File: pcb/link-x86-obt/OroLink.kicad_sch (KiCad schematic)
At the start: 7 parts, among them J1 67996-408HLF

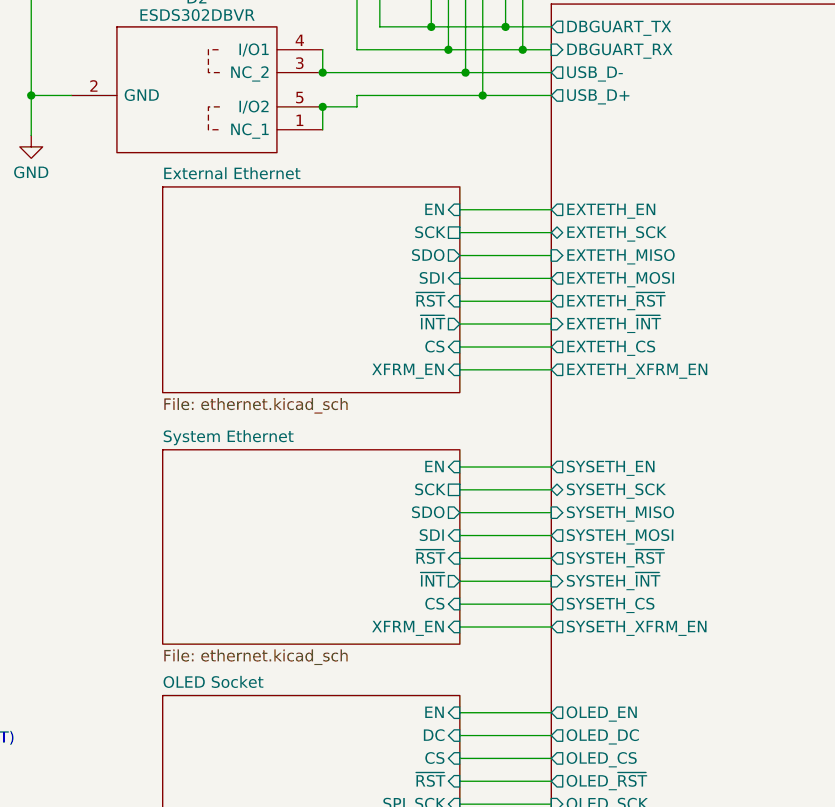
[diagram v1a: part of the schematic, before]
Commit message: omit ethernet enable mosfets in lieu of reset mosfet
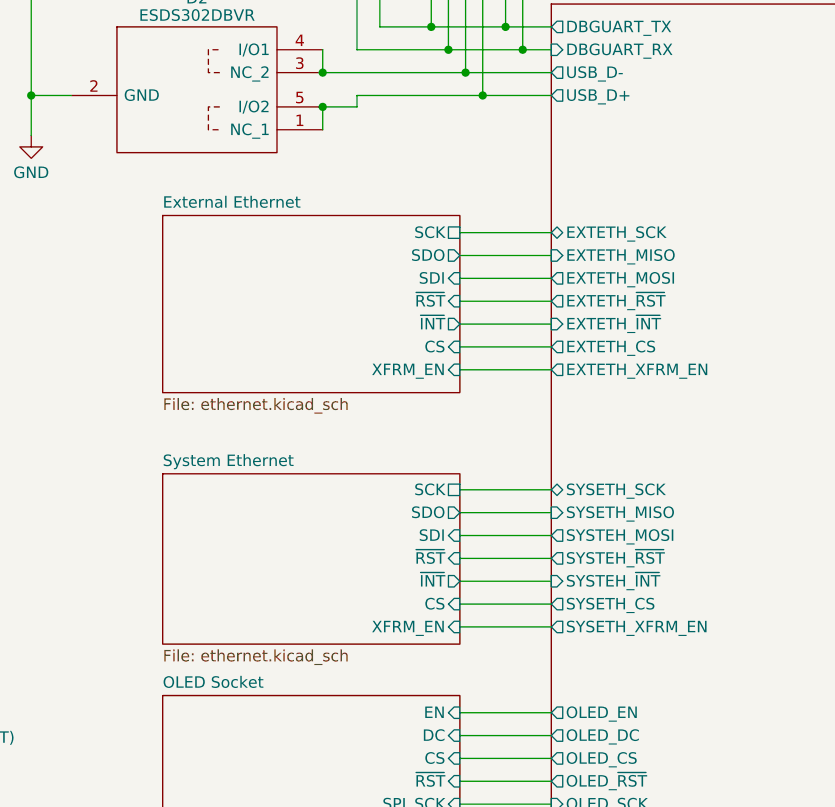
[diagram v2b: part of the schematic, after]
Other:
- sheet External Ethernet ports: added none; removed EN
- sheet Microcontroller ports: added none; removed EXTETH_EN, SYSETH_EN
- sheet System Ethernet ports: added none; removed EN
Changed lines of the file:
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@@
-	(wire
-		(pts
-			(xy 114.3 105.41) (xy 124.46 105.41)
-		)
-		(stroke
-			(width 0)
-			(type default)
-		)
-	)
 	(wire
 		(pts
@@
 		(pts
 			(xy 102.87 65.405) (xy 99.06 65.405)
-		)
-		(stroke
-			(width 0)
-			(type default)
-		)
-	)
-	(wire
-		(pts
-			(xy 114.3 76.835) (xy 124.46 76.835)
 		)
 		(stroke
@@
 	)
 	(sheet
-		(at 81.28 103.505)
-		(size 33.02 21.59)
+		(at 81.28 106.172)
+		(size 33.02 18.923)
 		(fields_autoplaced yes)
 		(stroke
@@
 		)
 		(property "Sheetname" "System Ethernet"
-			(at 81.28 102.7934 0)
+			(at 81.28 105.4604 0)
 			(effects
 				(font
@@
 		(pin "XFRM_EN" input
 			(at 114.3 123.19 0)
-			(effects
-				(font
-					(size 1.27 1.27)
-				)
-				(justify right)
-			)
-		)
-		(pin "EN" input
-			(at 114.3 105.41 0)
 			(effects
 				(font
@@
 	)
 	(sheet
-		(at 81.28 74.295)
-		(size 33.02 22.86)
+		(at 81.28 77.47)
+		(size 33.02 19.685)
 		(fields_autoplaced yes)
 		(stroke
@@
 		)
 		(property "Sheetname" "External Ethernet"
-			(at 81.28 73.5834 0)
+			(at 81.28 76.7584 0)
 			(effects
 				(font
@@
 		(pin "XFRM_EN" input
 			(at 114.3 94.615 0)
-			(effects
-				(font
-					(size 1.27 1.27)
-				)
-				(justify right)
-			)
-		)
-		(pin "EN" input
-			(at 114.3 76.835 0)
 			(effects
 				(font
@@
 			)
 		)
-		(pin "EXTETH_EN" output
-			(at 124.46 76.835 180)
-			(effects
-				(font
-					(size 1.27 1.27)
-				)
-				(justify left)
-			)
-		)
-		(pin "SYSETH_EN" output
-			(at 124.46 105.41 180)
-			(effects
-				(font
-					(size 1.27 1.27)
-				)
-				(justify left)
-			)
-		)

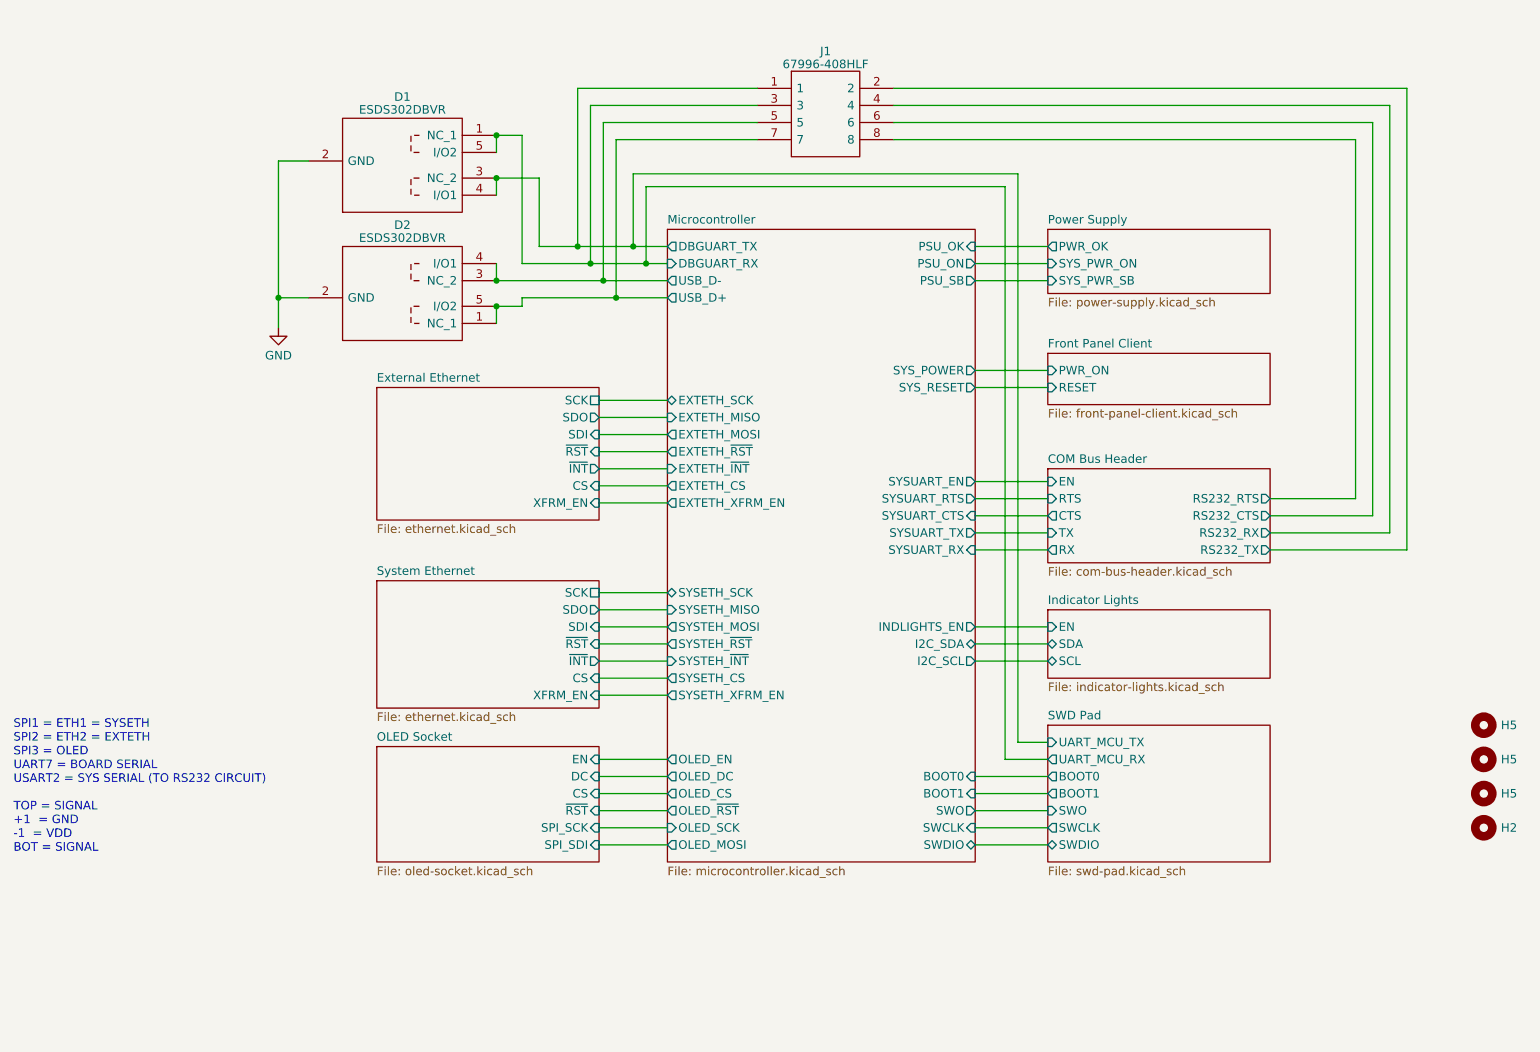
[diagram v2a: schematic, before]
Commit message: add VBUS and ground headers
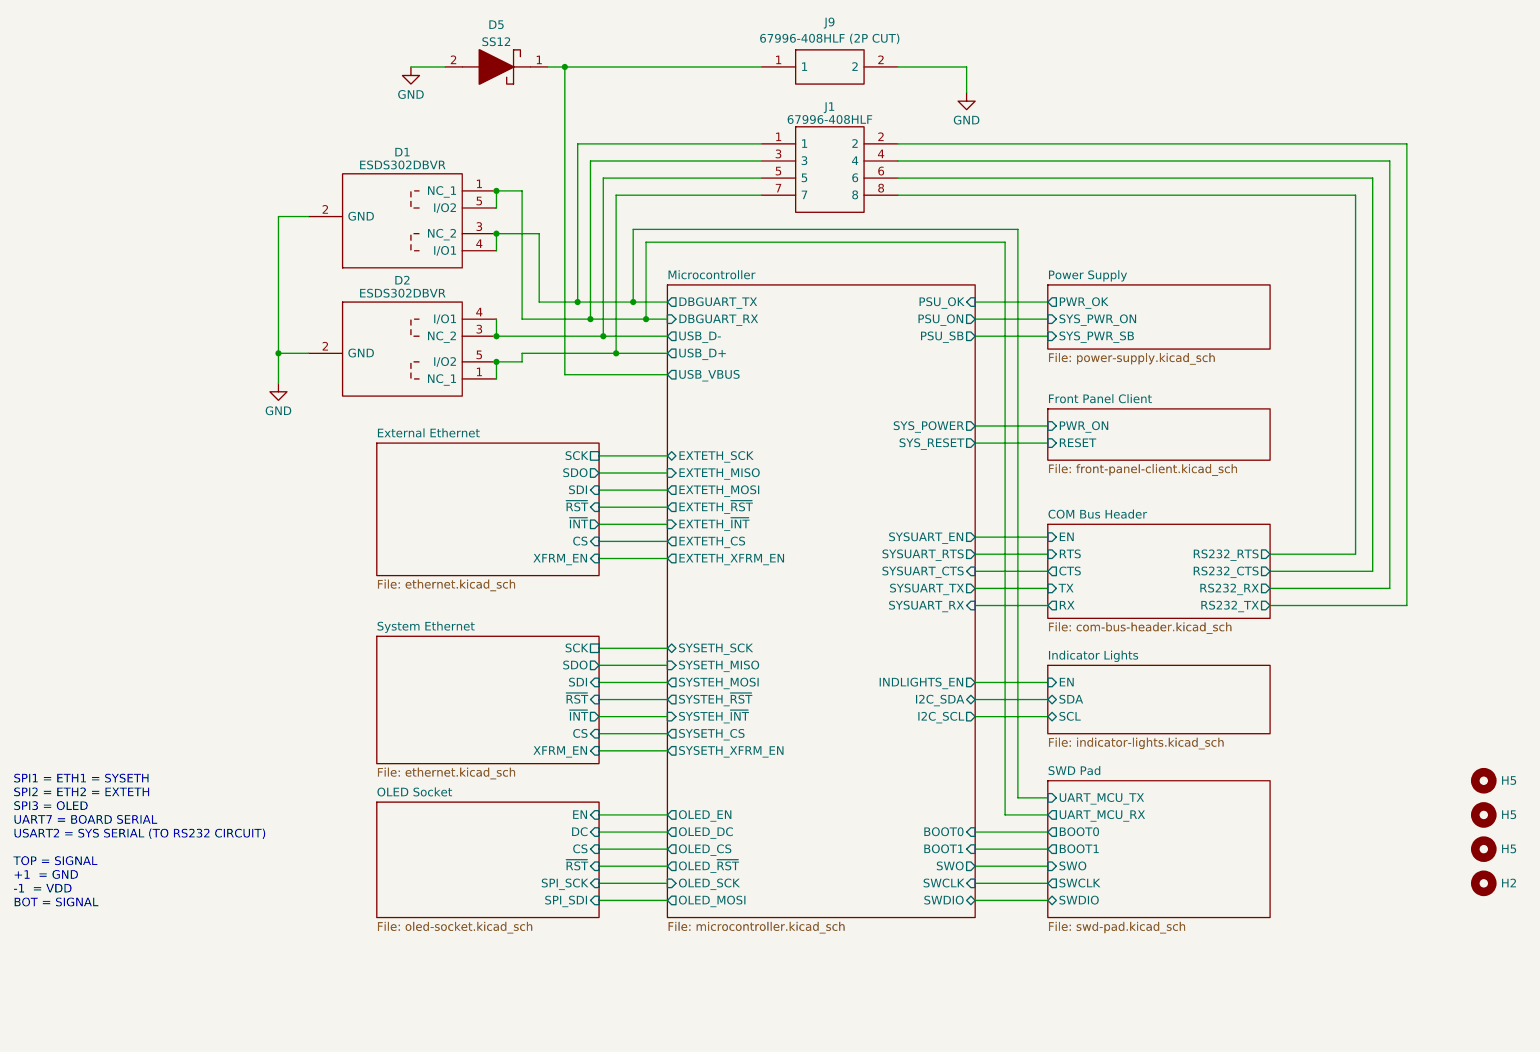
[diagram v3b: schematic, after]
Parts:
- added D5: SS12, Oro Footprints:DIOM5227X250N, symbol SamacSys_Parts:SS12
- added J9: 67996-408HLF (2P CUT), Oro Footprints:HDRV8W89P254_2X4_1016X483X858P_2P, symbol Oro (Legacy):67996-408HLF (2P Cut)
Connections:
- net GND: now also D5.2, J9.2
- new net Microcontroller/USB_VBUS: D5.1, J9.1
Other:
- sheet Microcontroller ports: added USB_VBUS; removed none
- moved on the sheet: D1, D2, H2, H5, J1

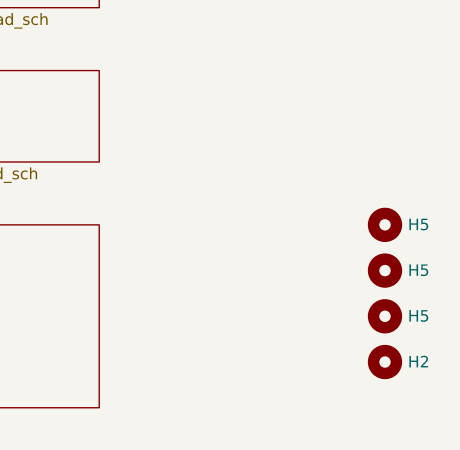
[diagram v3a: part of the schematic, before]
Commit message: make top right mounting hole grounded (closes #51)
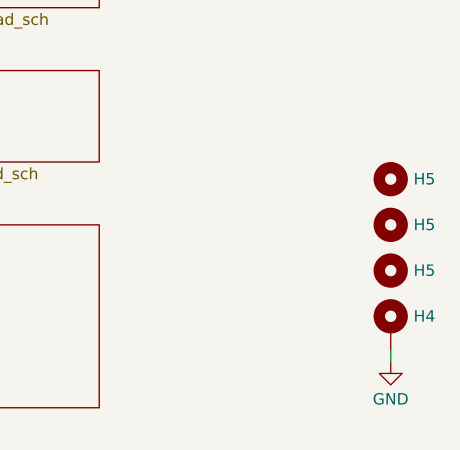
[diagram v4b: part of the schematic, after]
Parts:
- removed H2: MountingHole_Pad, MountingHole:MountingHole_3.2mm_M3_Pad_Via, symbol Mechanical:MountingHole
- added H4: MountingHole_Pad, MountingHole:MountingHole_3.2mm_M3_Pad_Via, symbol Mechanical:MountingHole_Pad
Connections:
- net GND: now also H4.1
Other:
- moved on the sheet: H5
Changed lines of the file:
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@@
+	(wire
+		(pts
+			(xy 246.38 149.86) (xy 246.38 151.13)
+		)
+		(stroke
+			(width 0)
+			(type default)
+		)
+	)
 	(wire
 		(pts
@@
 	(symbol
 		(lib_id "Mechanical:MountingHole")
-		(at 245.745 146.05 0)
+		(at 246.38 140.97 0)
 		(unit 1)
 		(exclude_from_sim yes)
@@
 		(dnp no)
 		(property "Reference" "H5"
-			(at 248.285 146.05 0)
+			(at 248.92 140.97 0)
 			(effects
 				(font
@@
 		)
 		(property "Value" "MountingHole_Pad"
-			(at 248.285 146.0573 0)
+			(at 248.92 140.9773 0)
 			(effects
 				(font
@@
 		)
 		(property "Footprint" "MountingHole:MountingHole_3.2mm_M3_Pad_Via"
-			(at 245.745 146.05 0)
+			(at 246.38 140.97 0)
 			(effects
 				(font
@@
 		)
 		(property "Datasheet" "~"
-			(at 245.745 146.05 0)
+			(at 246.38 140.97 0)
 			(effects
 				(font
@@
 		)
 		(property "Description" ""
-			(at 245.745 146.05 0)
+			(at 246.38 140.97 0)
 			(effects
 				(font
@@
 	(symbol
 		(lib_id "Mechanical:MountingHole")
-		(at 245.745 140.97 0)
+		(at 246.38 135.89 0)
 		(unit 1)
 		(exclude_from_sim yes)
@@
 		(dnp no)
 		(property "Reference" "H5"
-			(at 248.285 140.97 0)
+			(at 248.92 135.89 0)
 			(effects
 				(font
@@
 		)
 		(property "Value" "MountingHole_Pad"
-			(at 248.285 140.9773 0)
+			(at 248.92 135.8973 0)
 			(effects
 				(font
@@
 		)
 		(property "Footprint" "MountingHole:MountingHole_3.2mm_M3_Pad_Via"
-			(at 245.745 140.97 0)
+			(at 246.38 135.89 0)
 			(effects
 				(font
@@
 		)
 		(property "Datasheet" "~"
-			(at 245.745 140.97 0)
+			(at 246.38 135.89 0)
 			(effects
 				(font
@@
 		)
 		(property "Description" ""
-			(at 245.745 140.97 0)
+			(at 246.38 135.89 0)
 			(effects
 				(font
@@
 	(symbol
 		(lib_id "Mechanical:MountingHole")
-		(at 245.745 135.89 0)
+		(at 246.38 130.81 0)
 		(unit 1)
 		(exclude_from_sim yes)
@@
 		(dnp no)
 		(property "Reference" "H5"
-			(at 248.285 135.89 0)
+			(at 248.92 130.81 0)
 			(effects
 				(font
@@
 		)
 		(property "Value" "MountingHole_Pad"
-			(at 248.285 135.8973 0)
+			(at 248.92 130.8173 0)
 			(effects
 				(font
@@
 		)
 		(property "Footprint" "MountingHole:MountingHole_3.2mm_M3_Pad_Via"
-			(at 245.745 135.89 0)
+			(at 246.38 130.81 0)
 			(effects
 				(font
@@
 		)
 		(property "Datasheet" "~"
-			(at 245.745 135.89 0)
+			(at 246.38 130.81 0)
 			(effects
 				(font
@@
 		)
 		(property "Description" ""
-			(at 245.745 135.89 0)
+			(at 246.38 130.81 0)
 			(effects
 				(font
@@
 	)
 	(symbol
-		(lib_id "Mechanical:MountingHole")
-		(at 245.745 151.13 0)
-		(unit 1)
-		(exclude_from_sim yes)
-		(in_bom no)
-		(on_board yes)
-		(dnp no)
-		(property "Reference" "H2"
-			(at 248.285 151.1387 0)
-			(effects
-				(font
-					(size 1.27 1.27)
-				)
-				(justify left)
-			)
-		)
-		(property "Value" "MountingHole_Pad"
-			(at 248.285 151.1373 0)
-			(effects
-				(font
-					(size 1.27 1.27)
-				)
-				(justify left)
-				(hide yes)
-			)
-		)
-		(property "Footprint" "MountingHole:MountingHole_3.2mm_M3_Pad_Via"
-			(at 245.745 151.13 0)
-			(effects
-				(font
-					(size 1.27 1.27)
-				)
-				(hide yes)
-			)
-		)
-		(property "Datasheet" "~"
-			(at 245.745 151.13 0)
-			(effects
-				(font
-					(size 1.27 1.27)
-				)
-				(hide yes)
-			)
-		)
-		(property "Description" ""
-			(at 245.745 151.13 0)
-			(effects
-				(font
-					(size 1.27 1.27)
-				)
-				(hide yes)
-			)
-		)
-		(instances
-			(project "Oro Testbed v2"
-				(path "/3d0fc623-63eb-45e5-a304-e470d9b3a173"
-					(reference "H2")
-					(unit 1)
-				)
-			)
-			(project "OroLink"
-				(path "/e89dcd22-1250-4a5b-b778-1c95a0dd623d"
-					(reference "H4")
-					(unit 1)
-				)
-			)
-		)
-	)
-	(symbol
 		(lib_id "SamacSys_Parts:67996-408HLF")
 		(at 138.43 41.275 0)
@@
 					(unit 1)
 				)
+			)
+		)
+	)
+	(symbol
+		(lib_name "GND_1")
+		(lib_id "power:GND")
+		(at 246.38 151.13 0)
+		(unit 1)
+		(exclude_from_sim no)
+		(in_bom yes)
+		(on_board yes)
+		(dnp no)
+		(fields_autoplaced yes)
+		(property "Reference" "#PWR088"
+			(at 246.38 157.48 0)
+			(effects
+				(font
+					(size 1.27 1.27)
+				)
+				(hide yes)
+			)
+		)
+		(property "Value" "GND"
+			(at 246.38 155.2631 0)
+			(effects
+				(font
+					(size 1.27 1.27)
+				)
+			)
+		)
+		(property "Footprint" ""
+			(at 246.38 151.13 0)
+			(effects
+				(font
+					(size 1.27 1.27)
+				)
+				(hide yes)
+			)
+		)
+		(property "Datasheet" ""
+			(at 246.38 151.13 0)
+			(effects
+				(font
+					(size 1.27 1.27)
+				)
+				(hide yes)
+			)
+		)
+		(property "Description" "Power symbol creates a global label with name \"GND\" , ground"
+			(at 246.38 151.13 0)
+			(effects
+				(font
+					(size 1.27 1.27)
+				)
+				(hide yes)
+			)
+		)
+		(pin "1"
+		)
+		(instances
+			(project "OroLink"
+				(path "/e89dcd22-1250-4a5b-b778-1c95a0dd623d"
+					(reference "#PWR088")
+					(unit 1)
+				)
+			)
+		)
+	)
+	(symbol
+		(lib_id "Mechanical:MountingHole_Pad")
+		(at 246.38 147.32 0)
+		(unit 1)
+		(exclude_from_sim no)
+		(in_bom yes)
+		(on_board yes)
+		(dnp no)
+		(property "Reference" "H4"
+			(at 248.92 146.05 0)
+			(effects
+				(font
+					(size 1.27 1.27)
+				)
+				(justify left)
+			)
+		)
+		(property "Value" "MountingHole_Pad"
+			(at 248.92 147.2621 0)
+			(effects
+				(font
+					(size 1.27 1.27)
+				)
+				(justify left)
+				(hide yes)
+			)
+		)
+		(property "Footprint" "MountingHole:MountingHole_3.2mm_M3_Pad_Via"
+			(at 246.38 147.32 0)
+			(effects
+				(font
+					(size 1.27 1.27)
+				)
+				(hide yes)
+			)
+		)
+		(property "Datasheet" "~"
+			(at 246.38 147.32 0)
+			(effects
+				(font
+					(size 1.27 1.27)
+				)
+				(hide yes)
+			)
+		)
+		(property "Description" "Mounting Hole with connection"
+			(at 246.38 147.32 0)
+			(effects
+				(font
+					(size 1.27 1.27)
+				)
+				(hide yes)
+			)
+		)
+		(pin "1"
+		)
+		(instances
+			(project "OroLink"
+				(path "/e89dcd22-1250-4a5b-b778-1c95a0dd623d"
+					(reference "H4")
+					(unit 1)
+				)

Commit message: assembly update
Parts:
- H4, H5: now not fitted
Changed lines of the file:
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@@
 		(in_bom no)
 		(on_board yes)
-		(dnp no)
+		(dnp yes)
 		(property "Reference" "H5"
 			(at 248.92 140.97 0)
@@
 		(in_bom no)
 		(on_board yes)
-		(dnp no)
+		(dnp yes)
 		(property "Reference" "H5"
 			(at 248.92 135.89 0)
@@
 		(in_bom no)
 		(on_board yes)
-		(dnp no)
+		(dnp yes)
 		(property "Reference" "H5"
 			(at 248.92 130.81 0)
@@
 		(in_bom yes)
 		(on_board yes)
-		(dnp no)
+		(dnp yes)
 		(property "Reference" "H4"
 			(at 248.92 146.05 0)

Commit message: initial test of new board
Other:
- added sheet SD Port (sd-port.kicad_sch)
- sheet External Ethernet ports: added none; removed XFRM_EN
- sheet Microcontroller ports: added SD_CS, SD_EN, SD_HOST_SUT_SEL, SD_MISO, SD_MOSI, SD_SCK, SD_SUT_SENSE, SD_~{LED}; removed EXTETH_XFRM_EN, SYSETH_XFRM_EN
- sheet System Ethernet ports: added none; removed XFRM_EN
